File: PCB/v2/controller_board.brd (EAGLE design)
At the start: 160 x 100 mm, 30 parts, among them M1 B4B-PH-K-S(LF)(SN), M2 B4B-PH-K-S(LF)(SN), M3 B4B-PH-K-S(LF)(SN), M4 B4B-PH-K-S(LF)(SN)

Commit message: chore(pcb): improve schematics
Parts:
- added R8: 10kR, rcl:R0805
- moved R5 130.3 mm to (10.2, 61.0), turned to 90 degrees
- moved S1 128.7 mm to (5.08, 34.3), turned to 270 degrees
- moved R2 124.5 mm to (10.2, 34.3), turned to 90 degrees
- moved S4 121.8 mm to (5.08, 61.0), turned to 270 degrees
- moved R1 112.4 mm to (14.0, 29.2)
- moved R7 111.8 mm to (27.9, 30.5)
- moved R4 106.6 mm to (10.2, 52.1), turned to 90 degrees
- moved 24V_FUSE 101.5 mm to (66.0, 12.7)
- moved S3 97.9 mm to (5.08, 52.1), turned to 270 degrees
- moved R6 97.4 mm to (10.2, 72.4), turned to 90 degrees
- moved POWER_CONNECTOR 96.2 mm to (95.2, 21.6), turned to 90 degrees
- moved D2 89.7 mm to (83.8, 29.2)
- moved UART_1 83.9 mm to (27.9, 3.81)
- moved R3 83.2 mm to (10.2, 43.2), turned to 90 degrees
- moved D1 83.2 mm to (85.1, 12.7)
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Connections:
- net A3 renamed N$24
- removed net N$24 (its old number): D2.A, POWER_CONNECTOR.1
- removed net N$26: D1.A, POWER_CONNECTOR.4
- new net N$22: CONTROLLER.5, R1.2, R8.1, UART_1.2
- net GND: now also D1.A, D2.A, POWER_CONNECTOR.1, POWER_CONNECTOR.4; no longer MC4.16
- net UART: now also R8.2; no longer CONTROLLER.5, R1.2, UART_1.2
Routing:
- net 24V: track 292.5 -> 38.9 mm
- net GND: track 273.7 -> 54.2 mm
- net 5V: track 193.8 -> 72.0 mm, vias 0 -> 1
- net A0: track 137.2 -> 74.2 mm
- net N$25: track 0.00 -> 44.3 mm
- net N$23: track 0.00 -> 43.8 mm
- net N$15: track 0.00 -> 36.1 mm
- net N$24: track 58.0 -> 90.9 mm, vias 0 -> 2
- net N$11: track 0.00 -> 25.8 mm
- net N$7: track 0.00 -> 25.6 mm
- net N$2: track 0.00 -> 25.4 mm
- net N$1: track 0.00 -> 23.7 mm
- net N$9: track 0.00 -> 23.5 mm
- net N$5: track 0.00 -> 23.5 mm
- net N$14: track 0.00 -> 22.3 mm
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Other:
- board size 160 x 100 mm -> 100 x 80 mm

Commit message: feat(pcb): add ESD protection
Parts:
- removed DEBUG: B2B-PH-K-S(LF)(SN), B2B-PH-K-S_LF__SN_:JST_B2B-PH-K-S(LF)(SN)
- added C_M1_A1, C_M1_A2, C_M1_B1, C_M1_B2, C_M2_A1, C_M2_A2, C_M2_A3, C_M2_A4, C_M2_B1, C_M2_B2, C_M2_B3, C_M2_B4, C_M3_A1, C_M3_A2, C_M3_B1, C_M3_B2: 470pF 100V, rcl:C0402
- added R_M1_A, R_M1_B, R_M2_A, R_M2_A1, R_M2_B, R_M2_B1, R_M3_A, R_M3_B: S1210, varistor:S1210
- CONTROLLER: value TINY2040 -> TINY2040_HEADER; device pimoroni-boards:TINY2040 -> tiny2040_headerd:TINY2040_HEADER
- moved CONTROLLER 30.5 mm to (2.54, -16.5)
- renumbered MC1 to M1_TMC, MC2 to M2_TMC, MC3 to M3_TMC, MC4 to M4_TMC
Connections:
- removed net N$18 (its old number): CONTROLLER.SWCLK, DEBUG.2
- new net N$19: M1_TMC.5
- new net N$26: M1_TMC.4
- new net N$27: M1_TMC.6
- new net N$28: M2_TMC.4
- new net N$29: M2_TMC.5
- new net N$30: M2_TMC.6
- new net N$31: M2_TMC.3
- new net N$32: C_M2_A3.2, M4.1, R_M2_A1.1
- new net N$33: C_M2_A4.2, M4.2, R_M2_A1.2
- new net N$34: C_M2_B3.2, M4.3, R_M2_B1.1
- new net N$35: C_M2_B4.2, M4.4, R_M2_B1.2
- new net N$36: M4_TMC.4
- new net N$37: M4_TMC.5
- new net N$38: M4_TMC.6
- new net N$39: M4_TMC.3
- net GND: now also CONTROLLER.GND2, CONTROLLER.GND3, C_M1_A1.1, C_M1_A2.1, C_M1_B1.1, C_M1_B2.1, C_M2_A1.1, C_M2_A2.1, C_M2_A3.1, C_M2_A4.1, C_M2_B1.1, C_M2_B2.1, C_M2_B3.1, C_M2_B4.1, C_M3_A1.1, C_M3_A2.1, C_M3_B1.1, C_M3_B2.1
- net N$1: now also C_M1_A1.2, R_M1_A.1; no longer M1_TMC.5
- net N$10: now also C_M3_A2.2, M3.2, R_M3_A.2; no longer M3.4, M3_TMC.4
- net N$11: now also C_M3_B1.2, M3.3, R_M3_B.1; no longer M3.2, M3_TMC.6
- net N$12: now also C_M3_B2.2, M3.4, R_M3_B.2; no longer M3.3, M3_TMC.3
- net N$13: now also M3_TMC.4; no longer M4.1, M4_TMC.5
- net N$14: now also M3_TMC.5; no longer M4.4, M4_TMC.4
- net N$15: now also M3_TMC.6; no longer M4.2, M4_TMC.6
- net N$16: now also M3_TMC.3; no longer M4.3, M4_TMC.3
- net N$2: now also C_M1_A2.2, R_M1_A.2; no longer M1_TMC.6
- net N$21: now also M1_TMC.3; no longer CONTROLLER.SWDIO, DEBUG.1
- net N$3: now also C_M1_B1.2, R_M1_B.1; no longer M1_TMC.3
- net N$4: now also C_M1_B2.2, R_M1_B.2; no longer M1_TMC.4
- net N$5: now also C_M2_A1.2, R_M2_A.1; no longer M2_TMC.5
- net N$6: now also C_M2_A2.2, M2.2, R_M2_A.2; no longer M2.4, M2_TMC.4
- net N$7: now also C_M2_B1.2, M2.3, R_M2_B.1; no longer M2.2, M2_TMC.6
- net N$8: now also C_M2_B2.2, M2.4, R_M2_B.2; no longer M2.3, M2_TMC.3
- net N$9: now also C_M3_A1.2, R_M3_A.1; no longer M3_TMC.5
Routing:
- net N$15: track 36.1 -> 0.00 mm
- net N$11: track 25.8 -> 0.00 mm
- net N$7: track 25.6 -> 0.00 mm
- net N$2: track 25.4 -> 0.00 mm
- net N$1: track 23.7 -> 0.00 mm
- net N$9: track 23.5 -> 0.00 mm
- net N$5: track 23.5 -> 0.00 mm
- net N$14: track 22.3 -> 0.00 mm
- net N$13: track 21.9 -> 0.00 mm
- net N$10: track 21.0 -> 0.00 mm
- net N$6: track 19.0 -> 0.00 mm
- net N$4: track 18.6 -> 0.00 mm
- net N$12: track 18.0 -> 0.00 mm
- net N$8: track 17.0 -> 0.00 mm
- net N$3: track 16.9 -> 0.00 mm
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
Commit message: feat(pcb): add proper PCB layout
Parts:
- removed C_M1_A1, C_M1_A2, C_M1_B1, C_M1_B2, C_M2_A1, C_M2_A2, C_M2_A3, C_M2_A4, C_M2_B1, C_M2_B2, C_M2_B3, C_M2_B4, C_M3_A1, C_M3_A2, C_M3_B1, C_M3_B2: 470pF 100V, rcl:C0402
- removed R8: 10kR, rcl:R0805
- removed R_M1_A, R_M1_B, R_M2_A, R_M2_A1, R_M2_B, R_M2_B1, R_M3_A, R_M3_B: S1210, varistor:S1210
- added C1, C10, C11, C12, C13, C14, C15, C16, C2, C3, C4, C5, C6, C7, C8, C9: 470pF 100V, rcl:C0402
- added VR1, VR2, VR3, VR4, VR5, VR6, VR7, VR8: S1210, varistor:S1210
- moved LED 91.6 mm to (68.5, 6.38)
- moved R6 82.9 mm to (68.3, 13.2), turned to 180 degrees
- moved S4 77.0 mm to (59.3, 6.38)
- moved R5 68.4 mm to (59.1, 13.2), turned to 180 degrees
- moved R1 65.4 mm to (77.4, 13.2)
- moved S3 64.2 mm to (50.1, 6.38)
- moved SPI 56.1 mm to (96.6, 7.81), turned to 270 degrees
- moved R4 55.6 mm to (49.9, 13.2), turned to 180 degrees
- moved D2 55.0 mm to (133.8, 6.21)
- moved 5V_FUSE 54.1 mm to (115.0, 6.21)
- moved S2 51.4 mm to (40.9, 6.38)
- moved M1_TMC 49.6 mm to (135.6, 37.9), turned to 270 degrees
- moved UART_1 49.6 mm to (77.4, 6.38), turned to 270 degrees
- moved 24V_FUSE 49.5 mm to (115.0, 19.7)
- moved D1 49.5 mm to (134.1, 19.7)
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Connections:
- removed net N$22: CONTROLLER.5, R1.2, R8.1, UART_1.2
- net GND: now also C1.1, C10.1, C11.1, C12.1, C13.1, C14.1, C15.1, C16.1, C2.1, C3.1, C4.1, C5.1, C6.1, C7.1, C8.1, C9.1; no longer C_M1_A1.1, C_M1_A2.1, C_M1_B1.1, C_M1_B2.1, C_M2_A1.1, C_M2_A2.1, C_M2_A3.1, C_M2_A4.1, C_M2_B1.1, C_M2_B2.1, C_M2_B3.1, C_M2_B4.1, C_M3_A1.1, C_M3_A2.1, C_M3_B1.1, C_M3_B2.1
- net N$1: now also C1.2, VR1.1; no longer C_M1_A1.2, R_M1_A.1
- net N$10: now also C10.2, VR5.2; no longer C_M3_A2.2, R_M3_A.2
- net N$11: now also C11.2, VR6.1; no longer C_M3_B1.2, R_M3_B.1
- net N$12: now also C12.2, VR6.2; no longer C_M3_B2.2, R_M3_B.2
- net N$2: now also C2.2, VR1.2; no longer C_M1_A2.2, R_M1_A.2
- net N$3: now also C3.2, VR2.1; no longer C_M1_B1.2, R_M1_B.1
- net N$32: now also C13.2, VR7.1; no longer C_M2_A3.2, R_M2_A1.1
- net N$33: now also C14.2, VR7.2; no longer C_M2_A4.2, R_M2_A1.2
- net N$34: now also C15.2, VR8.1; no longer C_M2_B3.2, R_M2_B1.1
- net N$35: now also C16.2, VR8.2; no longer C_M2_B4.2, R_M2_B1.2
- net N$4: now also C4.2, VR2.2; no longer C_M1_B2.2, R_M1_B.2
- net N$5: now also C5.2, VR3.1; no longer C_M2_A1.2, R_M2_A.1
- net N$6: now also C6.2, VR3.2; no longer C_M2_A2.2, R_M2_A.2
- net N$7: now also C7.2, VR4.1; no longer C_M2_B1.2, R_M2_B.1
- net N$8: now also C8.2, VR4.2; no longer C_M2_B2.2, R_M2_B.2
- net N$9: now also C9.2, VR5.1; no longer C_M3_A1.2, R_M3_A.1
- net UART: now also CONTROLLER.5, R1.2, UART_1.2; no longer R8.2
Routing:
- net N$24: track 90.9 -> 0.00 mm, vias 2 -> 0
- net A2: track 84.8 -> 0.00 mm, vias 3 -> 0
- net A0: track 74.2 -> 0.00 mm
- net 5V: track 72.0 -> 0.00 mm, vias 1 -> 0
- net A1: track 59.9 -> 0.00 mm, vias 1 -> 0
- net GND: track 54.2 -> 0.00 mm
- net N$25: track 44.3 -> 0.00 mm
- net N$23: track 43.8 -> 0.00 mm
- net 24V: track 38.9 -> 0.00 mm
- net N$17: track 5.69 -> 0.00 mm
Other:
- board size 100 x 80 mm -> 150 x 66 mm

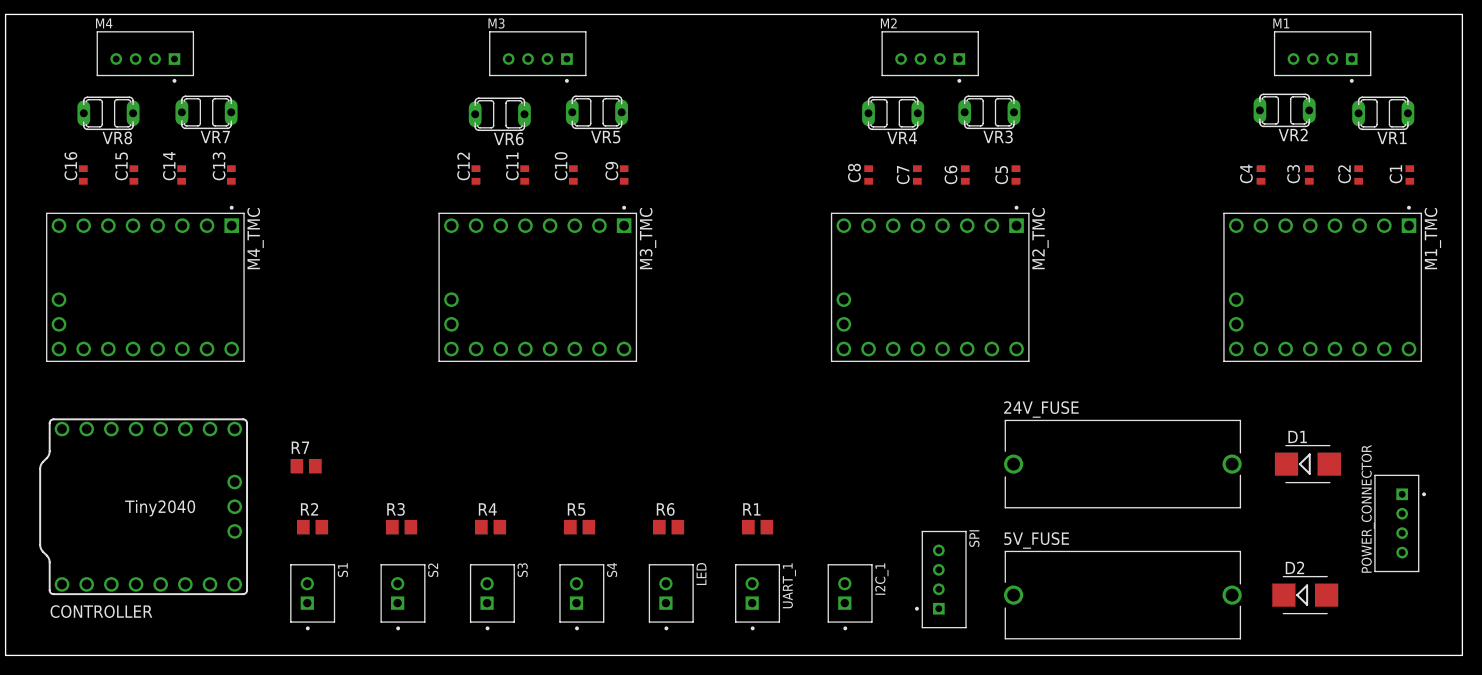
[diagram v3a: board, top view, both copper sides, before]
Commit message: feat(pcb): add wires
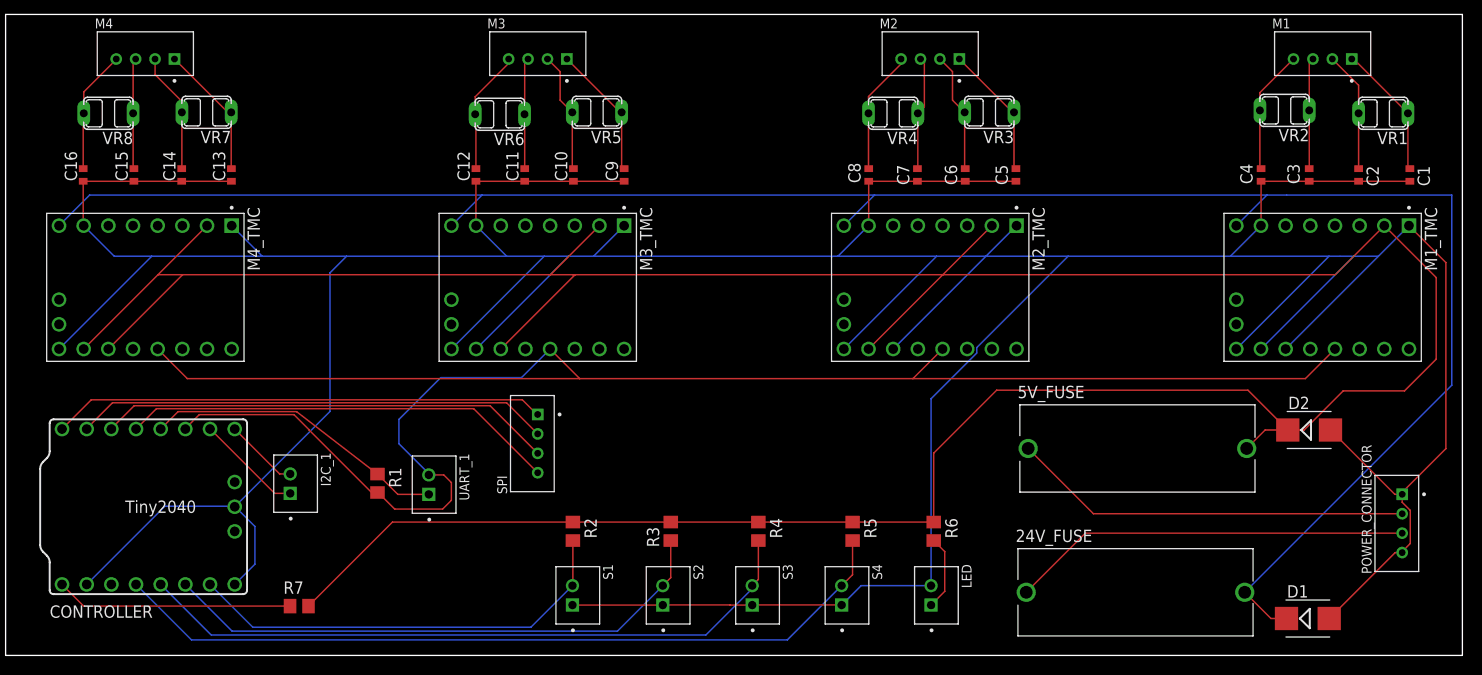
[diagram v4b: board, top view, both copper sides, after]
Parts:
- moved I2C_1 58.2 mm to (29.9, 17.7)
- moved SPI 44.7 mm to (54.2, 21.8), turned to 90 degrees
- moved R1 39.4 mm to (38.3, 17.7), turned to 270 degrees
- moved UART_1 35.1 mm to (44.1, 17.6)
- moved R5 28.1 mm to (87.2, 12.8), turned to 90 degrees
- moved R3 27.7 mm to (68.5, 12.8), turned to 90 degrees
- moved R4 27.6 mm to (77.5, 12.8), turned to 90 degrees
- moved R6 27.3 mm to (95.6, 12.8), turned to 90 degrees
- moved S1 27.3 mm to (58.9, 6.18)
- moved S2 27.3 mm to (68.2, 6.18)
- moved S3 27.3 mm to (77.4, 6.18)
- moved S4 27.3 mm to (86.6, 6.18)
- moved LED 27.3 mm to (95.8, 6.18)
- moved R2 26.8 mm to (58.4, 12.8), turned to 90 degrees
- moved D2 17.0 mm to (134.2, 23.2)
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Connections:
- net GND: now also M4_TMC.16
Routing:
- net GND: track 0.00 -> 548.1 mm
- net 5V: track 0.00 -> 348.2 mm
- net 24V: track 0.00 -> 213.2 mm
- net UART: track 0.00 -> 194.9 mm
- net N$24: track 0.00 -> 82.4 mm
- net A2: track 0.00 -> 70.3 mm
- net A1: track 0.00 -> 58.1 mm
- net RX: track 0.00 -> 50.9 mm
- net CS: track 0.00 -> 48.9 mm
- net SCK: track 0.00 -> 47.0 mm
- net A0: track 0.00 -> 45.6 mm
- net TX: track 0.00 -> 45.0 mm
- net N$23: track 0.00 -> 41.3 mm
- net N$25: track 0.00 -> 41.2 mm
- net N$20: track 0.00 -> 31.4 mm
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
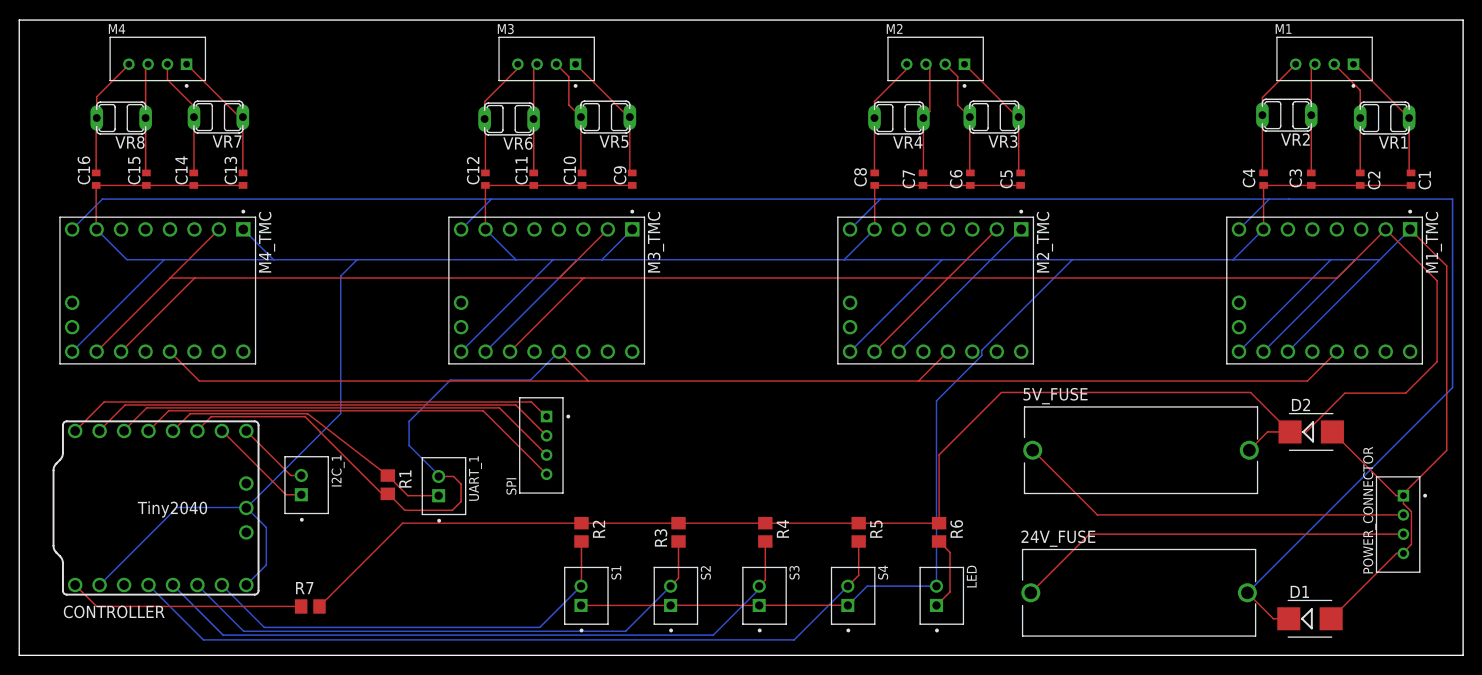
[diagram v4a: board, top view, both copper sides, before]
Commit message: feat(pcb): add 3V3 circuit
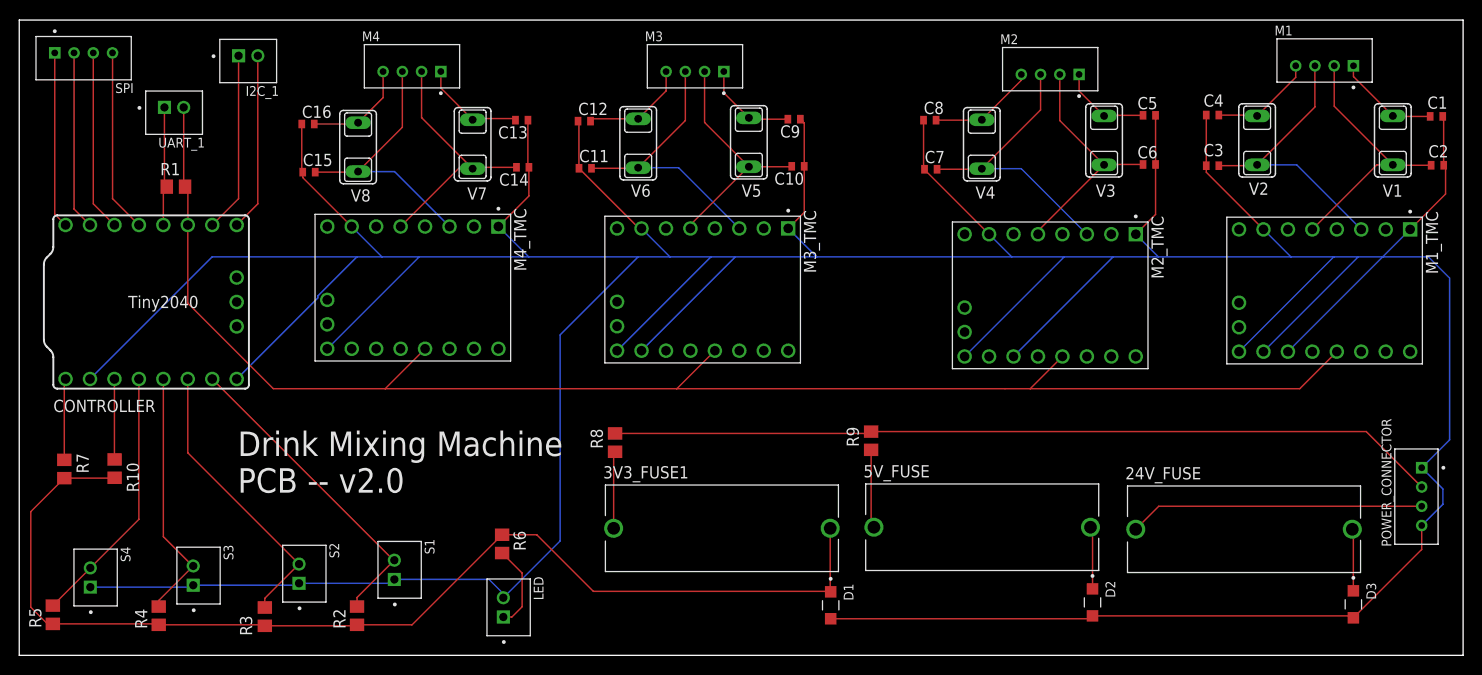
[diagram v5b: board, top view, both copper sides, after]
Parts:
- removed VR1, VR2, VR3, VR4, VR5, VR6, VR7, VR8: S1210, varistor:S1210
- added 3V3_FUSE1: 4628, 4628:FUSE_4628
- added D3: PTVS24VS1UR, PTVS24VS1UR:TVS_PTVS24VS1UR
- added R10, R8, R9: 0R, rcl:R0805
- added V1, V2, V3, V4, V5, V6, V7, V8: S2220, varistor:S2220
- D1: value 26V -> PTVS3V3S1UR; device diode:SMB -> PTVS3V3S1UR:TVS_PTVS3V3S1UR
- D2: value 1N5908 -> PTVS5V0S1UR; device diode:SMB -> PTVS5V0S1UR:TVS_PTVS5V0S1UR
- moved R5 84.2 mm to (3.49, 4.22), turned to 270 degrees
- moved S4 78.7 mm to (7.93, 8.09)
- moved R4 63.6 mm to (14.5, 4.12), turned to 270 degrees
- moved SPI 62.3 mm to (6.69, 62.0), turned to 180 degrees
- moved S3 58.8 mm to (18.6, 8.29)
- moved D1 49.8 mm to (84.3, 5.20), turned to 270 degrees
- moved UART_1 47.9 mm to (16.1, 56.4), turned to 180 degrees
- moved R6 45.4 mm to (50.2, 11.6)
- moved LED 45.0 mm to (50.8, 4.99)
- moved I2C_1 44.5 mm to (23.8, 61.7), turned to 180 degrees
- moved R3 43.9 mm to (25.5, 4.02), turned to 270 degrees
- moved S2 38.7 mm to (29.6, 8.48)
- moved R1 38.0 mm to (16.3, 48.7), turned to 0 degrees
- moved C14 34.2 mm to (52.3, 50.7), turned to 180 degrees
- moved C13 29.6 mm to (52.2, 55.6), turned to 180 degrees
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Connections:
- removed net 5V: 5V_FUSE.2, D2.C, M1_TMC.2, M2_TMC.15, M2_TMC.2, M3_TMC.14, M3_TMC.2, M4_TMC.14, M4_TMC.15, M4_TMC.2, R2.2, R3.2, R4.2, R5.2, R6.2, R7.2
- removed net N$28: M2_TMC.4
- removed net N$29: M2_TMC.5
- removed net N$30: M2_TMC.6
- removed net N$31: M2_TMC.3
- removed net N$32: C13.2, M4.1, VR7.1
- removed net N$33: C14.2, M4.2, VR7.2
- removed net N$34: C15.2, M4.3, VR8.1
- removed net N$35: C16.2, M4.4, VR8.2
- removed net N$36: M4_TMC.4
- removed net N$37: M4_TMC.5
- removed net N$38: M4_TMC.6
- removed net N$39: M4_TMC.3
- removed net N$9: C9.2, M3.1, VR5.1
- new net LOW_POWER: 3V3_FUSE1.2, 5V_FUSE.2, D1.C, D2.C, M1_TMC.2, M2_TMC.15, M2_TMC.2, M3_TMC.14, M3_TMC.2, M4_TMC.14, M4_TMC.15, M4_TMC.2, R10.2, R2.2, R3.2, R4.2, R5.2, R6.2, R7.2
- net 24V: now also D3.C; no longer D1.C
- net GND: now also D3.A; no longer CONTROLLER.GND3
- net N$1: now also POWER_CONNECTOR.2, R8.2, R9.2; no longer C1.2, M1.1, VR1.1
- net N$10: now also C12.2, M3.4, M3_TMC.6, V6.1; no longer C10.2, M3.2, VR5.2
- net N$11: now also M3_TMC.3, V6.2; no longer VR6.1
- net N$12: now also C9.2, M3.1, M3_TMC.4, V5.2; no longer C12.2, M3.4, VR6.2
- net N$13: now also C14.2, M4.2, M4_TMC.5, V7.1; no longer M3_TMC.4
- net N$14: now also C10.2, M3.2, V5.1
- net N$15: now also C16.2, M4.4, M4_TMC.6, V8.1; no longer M3_TMC.6
- net N$16: now also C15.2, M4.3, M4_TMC.3, V8.2; no longer M3_TMC.3
- net N$19: now also C3.2, M1.3, M1_TMC.3, V2.2; no longer M1_TMC.5
- net N$2: now also M1_TMC.5, V1.1; no longer VR1.2
- net N$21: now also 3V3_FUSE1.1, R8.1; no longer M1_TMC.3
- net N$22: now also C13.2, M4.1, M4_TMC.4, V7.2; no longer M1_TMC.4
- net N$23: now also CONTROLLER.3V3, R10.1; no longer 5V_FUSE.1, POWER_CONNECTOR.2
- net N$26: now also C1.2, M1.1, M1_TMC.4, V1.2; no longer M1_TMC.6
- net N$3: now also 5V_FUSE.1, R9.1; no longer C3.2, M1.3, VR2.1
- net N$4: now also M1_TMC.6, V2.1; no longer VR2.2
- net N$5: now also C6.2, M2.2, M2_TMC.5, V3.1; no longer C5.2, M2.1, VR3.1
- net N$6: now also C8.2, M2.4, M2_TMC.6, V4.1; no longer C6.2, M2.2, VR3.2
- net N$7: now also M2_TMC.3, V4.2; no longer VR4.1
- net N$8: now also C5.2, M2.1, M2_TMC.4, V3.2; no longer C8.2, M2.4, VR4.2
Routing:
- net LOW_POWER: track 0.00 -> 391.1 mm
- net 5V: track 348.2 -> 0.00 mm
- net N$1: track 13.9 -> 86.3 mm
- net 24V: track 213.2 -> 157.9 mm
- net N$24: track 82.4 -> 27.2 mm
- net GND: track 548.1 -> 597.6 mm
- net A2: track 70.3 -> 26.4 mm
- net UART: track 194.9 -> 161.4 mm
- net N$23: track 41.3 -> 8.36 mm
- net RX: track 50.9 -> 18.3 mm
- net N$19: track 0.00 -> 30.4 mm
- net CS: track 48.9 -> 18.6 mm
- net N$16: track 0.00 -> 28.6 mm
- net SCK: track 47.0 -> 18.8 mm
- net A1: track 58.1 -> 30.0 mm
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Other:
- board text added: "Drink Mixing Machine PCB -- v2.0"
